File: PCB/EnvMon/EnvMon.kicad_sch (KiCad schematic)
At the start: 40 parts, among them J1 USB-C, J2 DC, J3 TEMP, J4 Shelly, M1 OLED1.5-RGB, SW1 SW_Push, SW2 SW_Push, SW3 SW_Push, U1 LMR16006XDDCR, U2 SCD41, U3 FT231XQ, U4 ESP32-PICO-MINI-02, U5 QR, U7 SHT40, U8 VEML6040

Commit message: One board
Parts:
- removed C1: 100nF, RevK:C_0603_, symbol RevK:Hidden
- removed C2: 2.2uF, RevK:C_0805_, symbol RevK:Hidden
- removed C3: 10uF, RevK:C_0805_, symbol RevK:Hidden
- removed C4: 10nF, RevK:C_0603, symbol Device:C
- removed D1: Schottky, RevK:D_1206_, symbol RevK:Hidden
- removed D3: LED_BARG, RevK:MHS190RGBCT, symbol Device:LED_BARG
- removed D4: D, RevK:D_1206, symbol Device:D
- removed J4: Shelly, RevK:Shelly, symbol RevK:Shelly
- removed L1: 6.8uH, RevK:L_4x4_, symbol RevK:Hidden
- removed R10: 4k7, RevK:R_0603, symbol Device:R
- removed R11, R12: 10k, RevK:R_0603, symbol Device:R
- removed R6: 27R, RevK:R_0603, symbol Device:R
- removed R7: 300R, RevK:R_0603, symbol Device:R
- removed R8: 1K, RevK:R_0603, symbol Device:R
- removed R9: 100R, RevK:R_0603, symbol Device:R
- removed U1: LMR16006XDDCR, RevK:SOT-23-Thin-6-Reg, symbol RevK:LMR16006XDDCR
- removed U3: FT231XQ, RevK:QFN-20-1EP_4x4mm_P0.5mm_EP2.5x2.5mm, symbol RevK:FT231XQ
- removed U4: ESP32-PICO-MINI-02, RevK:ESP32-PICO-MINI-02, symbol RevK:ESP32-PICO-MINI-02
- added C1: 100nF, RevK:C_0402, symbol Device:C
- added C2: 22uF, RevK:C_0402, symbol Device:C
- added C3: 1uF, RevK:C_0402, symbol Device:C
- added C6: 10uF 50V, RevK:C_0603_, symbol RevK:Hidden
- added C7: 10uF 6.3V, RevK:C_0603_, symbol RevK:Hidden
- added C8: 100nF, RevK:C_0603_, symbol RevK:Hidden
- added D1: RGB, RevK:LED-RGB-1.6x1.6, symbol Device:LED_RGBA
- added D3: D, RevK:D_SOD-123, symbol Device:D
- added J5: Shelly, RevK:Shelly, symbol RevK:Shelly
- added L2: 10uH, RevK:L_4x4_, symbol RevK:Hidden
- added R14: 124k, RevK:R_0402_, symbol RevK:Hidden
- added R15: 39k2, RevK:R_0402_, symbol RevK:Hidden
- added R16: 1M, RevK:R_0402_, symbol RevK:Hidden
- added R17: 220R, RevK:R_0402, symbol Device:R
- added U1: ESP32-S3-MINI-1, RevK:ESP32-S3-MINI-1, symbol RevK:ESP32-S3-MINI-1-N4R2
- added U6: MD8942, RevK:SOT-23-6-MD8942, symbol RevK:MD89420-RegBlock
- C5: footprint RevK:C_0603 -> RevK:C_0402
- D2: footprint RevK:D_1206 -> RevK:D_SOD-123; LCSC Part # C143805 -> C1884542
- R1: value 100k 1% -> 680R; footprint RevK:R_0603 -> RevK:R_0402; LCSC Part # C14675 -> (none)
- R13, R3, R4: footprint RevK:R_0603 -> RevK:R_0402
- R2: value 30k 1% -> 2K; footprint RevK:R_0603 -> RevK:R_0402; LCSC Part # C100001 -> (none)
- R5: value 27R -> 10K; footprint RevK:R_0603 -> RevK:R_0402
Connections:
- net +3.3V: now also R5.1, C1.1, C2.1, D1.4 (A), J5.3 (3V3), U1.3 (3V3), U6.8 (VOUT); no longer R1.1
- net B: now also R17.2, U1.38 (GPIO42)
- net BUTTON1: now also U1.8 (GPIO4)
- net BUTTON2: now also U1.9 (GPIO5)
- net BUTTON3: now also U1.10 (GPIO6)
- net D+: now also J1.A6 (D+), J1.B6 (D+), U1.24 (GPIO20)
- net D-: now also J1.A7 (D-), J1.B7 (D-), U1.23 (GPIO19); no longer R5.2
- net DC: now also D3.1 (K), U6.5 (VIN)
- net G: now also R2.2, U1.36 (GPIO40)
- net GND: now also C1.2, C2.2, C3.2, J5.1 (GND), U1.1 (GND), U1.2 (GND), U1.42 (GND), U1.43 (GND), U1.46 (GND), U1.47 (GND), U1.48 (GND), U1.49 (GND), U1.50 (GND), U1.51 (GND), U1.52 (GND), U1.53 (GND), U1.54 (GND), U1.55 (GND), U1.56 (GND), U1.57 (GND), U1.58 (GND), U1.59 (GND), U1.60 (GND), U1.61 (GND), U1.62 (GND), U1.63 (GND), U1.64 (GND), U1.65 (GND), U6.2 (GND), U6.7 (GND); no longer R2.1
- net OLED-CS: now also U1.13 (GPIO9)
- net OLED-DC: now also U1.14 (GPIO10)
- net OLED-MOSI: now also U1.11 (GPIO7)
- net OLED-RST: now also U1.15 (GPIO11)
- net OLED-SCK: now also U1.12 (GPIO8)
- net R: now also R1.2, U1.37 (GPIO41)
- net SCL: now also U1.34 (GPIO38)
- net SDA: now also U1.35 (GPIO39)
- net TEMP: now also U1.16 (GPIO12)
- net at J2.2 (DC): now also D2.2 (A)
- net VBUS: no longer names the net of J1.A4 (VBUS), J1.A9 (VBUS), J1.B4 (VBUS), J1.B9 (VBUS)
- net VBUS: now also D3.2 (A); no longer D2.2 (A)
- new net: J5.2 (0), U1.4 (GPIO0)
- new net: J5.4 (Rx), U1.40 (GPIO44)
- new net: J5.5 (Tx), U1.39 (GPIO43)
- new net: D1.2 (GK), R2.1
- new net: C3.1, R5.2, U1.45 (EN)
- new net: D1.1 (RK), R1.1
- new net: D1.3 (BK), R17.1
- new net RX: U1.25 (GPIO21)
- new net TX: U1.27 (GPIO47)
- no-connect marks 13 -> 15

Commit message: WS2812B LED
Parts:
- removed D1: RGB, RevK:LED-RGB-1.6x1.6, symbol Device:LED_RGBA
- removed R1: 680R, RevK:R_0402, symbol Device:R
- removed R17: 220R, RevK:R_0402, symbol Device:R
- removed R2: 2K, RevK:R_0402, symbol Device:R
- added D4: XL-1010RGBC-WS2812B, RevK:SMD1010, symbol RevK:WS2812B-1mm
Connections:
- net +3.3V: now also D4.2 (+)
- net GND: now also D4.3 (-)
- net LED: now reaches U1.41 (GPIO45)
- net LED: now also D4.4 (I)
- net B: no longer names the net of U1.38 (GPIO42)
- net G: no longer names the net of U1.36 (GPIO40)
- net R: no longer names the net of U1.37 (GPIO41)
- no-connect marks 15 -> 19
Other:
- moved on the sheet: C3, R5

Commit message: New
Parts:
- removed D2: D, RevK:D_SOD-123, symbol Device:D
- added D2: Schottky, RevK:D_1206, symbol Diode:1N5819
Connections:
- net DC: now also D2.1 (K)
- net at J2.2 (DC): now also D2.2 (A)
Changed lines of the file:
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@@
-    )
-  )
-  (symbol (lib_id "Device:D") (at 44.45 123.825 0) (unit 1)
-    (in_bom yes) (on_board yes) (dnp no)
-    (property "Reference" "D2" (at 44.45 129.3368 0)
-      (effects (font (size 1.27 1.27)))
-    )
-    (property "Value" "D" (at 44.45 127.0254 0)
-      (effects (font (size 1.27 1.27)))
-    )
-    (property "Footprint" "RevK:D_SOD-123" (at 44.45 123.825 0)
-      (effects (font (size 1.27 1.27)) hide)
-    )
-    (property "Datasheet" "~" (at 44.45 123.825 0)
-      (effects (font (size 1.27 1.27)) hide)
-    )
-    (property "LCSC Part #" "C1884542" (at 44.45 123.825 0)
-      (effects (font (size 1.27 1.27)) hide)
-    )
-    (pin "1")
-    (pin "2")
-    (instances
-      (project "EnvMon"
-        (path "/12422a89-3d0c-485c-9386-f77121fd68fd"
-          (reference "D2") (unit 1)
-        )
-      )
-      (project "Access"
-        (path "/2a267270-6585-45e3-a633-b53049f10066"
-          (reference "D8") (unit 1)
-        )
-      )
-      (project "GenericS3"
-        (path "/2d210a96-f81f-42a9-8bf4-1b43c11086f3"
-          (reference "D1") (unit 1)
-        )
-      )
     )
   )
@@
         )
       )
+    )
+  )
+  (symbol (lib_id "Diode:1N5819") (at 44.45 123.825 0) (unit 1)
+    (in_bom yes) (on_board yes) (dnp no)
+    (property "Reference" "D2" (at 45.72 128.905 0)
+      (effects (font (size 1.27 1.27)))
+    )
+    (property "Value" "Schottky" (at 42.545 127 0)
+      (effects (font (size 1.27 1.27)))
+    )
+    (property "Footprint" "RevK:D_1206" (at 44.45 128.27 0)
+      (effects (font (size 1.27 1.27)) hide)
+    )
+    (property "Datasheet" "" (at 44.45 123.825 0)
+      (effects (font (size 1.27 1.27)) hide)
+    )
+    (property "LCSC Part #" "C143805" (at 44.45 123.825 0)
+      (effects (font (size 1.27 1.27)) hide)
+    )
+    (pin "1")
+    (pin "2")
+    (instances
+      (project "EnvMon"
+        (path "/12422a89-3d0c-485c-9386-f77121fd68fd"
+          (reference "D2") (unit 1)
+        )
+      )
+      (project "EPD75"
+        (path "/46c350bb-7de4-4e81-aafd-4af55e37aab0"
+          (reference "D6") (unit 1)
+        )
+      )

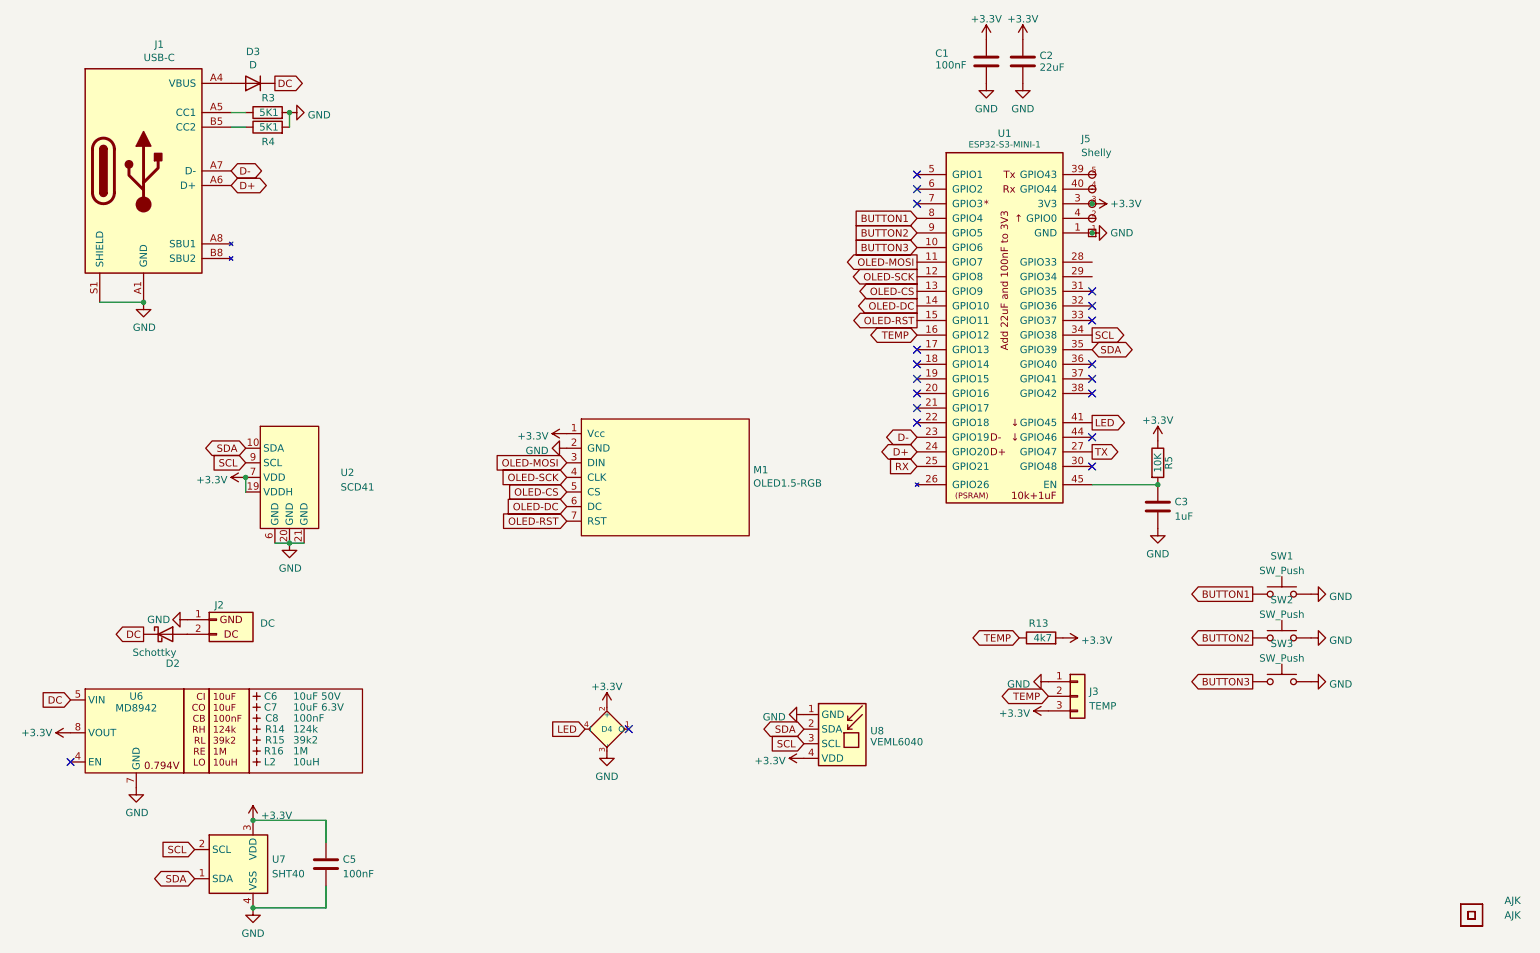
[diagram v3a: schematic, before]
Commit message: New plugs
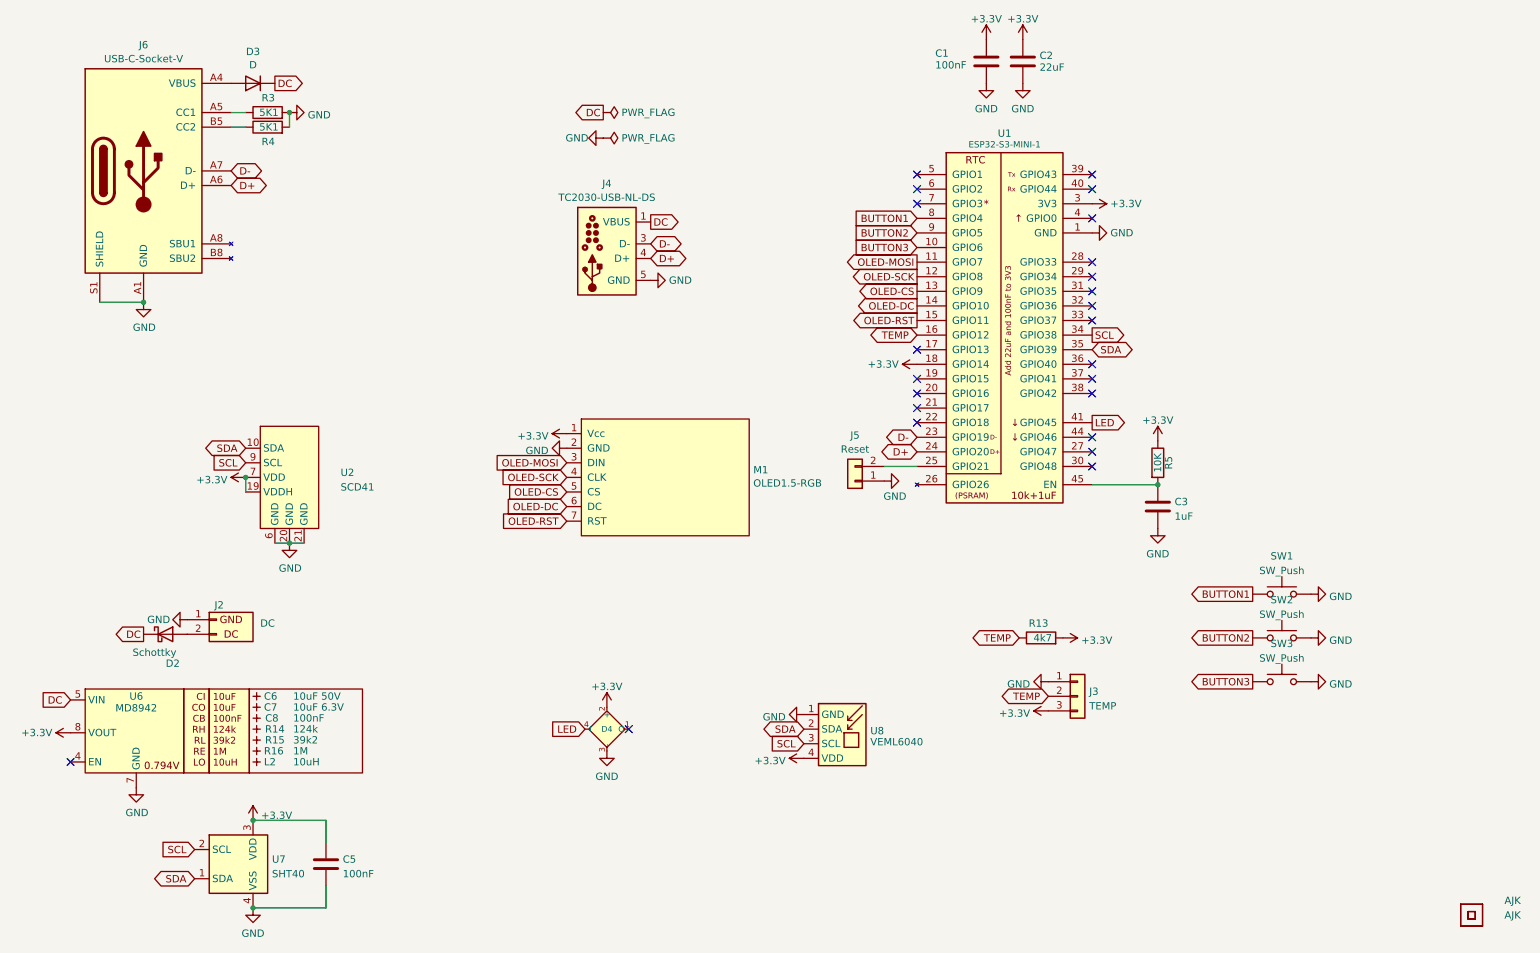
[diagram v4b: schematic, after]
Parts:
- removed J1: USB-C, RevK:USC16-TR, symbol RevK:USB-C
- removed J5: Shelly, RevK:Shelly, symbol RevK:Shelly
- added J4: TC2030-USB-NL-DS, RevK:Tag-Connect_TC2030-IDC-NL_2x03_P1.27mm_Vertical, symbol RevK:TC2030-USB-NL
- added J5: Reset, RevK:AA-Pad, symbol Connector_Generic:Conn_01x02
- added J6: USB-C-Socket-V, RevK:USB-C-Socket-H, symbol RevK:USB-C-Socket-H
- J2: footprint RevK:PTSM-HH-2-RA-W -> RevK:WAGO-2060-452-998-404
- J3: footprint RevK:PTSM-HH-3-RA -> RevK:WAGO-2060-453-998-404
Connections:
- net +3.3V: now also U1.18 (GPIO14)
- net D+: now also J4.4 (D+), J6.A6 (D+), J6.B6 (D+)
- net D-: now also J4.3 (D-), J6.A7 (D-), J6.B7 (D-)
- net DC: now also J4.1 (VBUS), J4.2 (VBUS)
- net GND: now also J4.5 (GND), J4.6 (GND), J5.1 (Pin_1), J6.A1 (GND), J6.A12 (GND), J6.B1 (GND), J6.B12 (GND), J6.S1 (SHIELD)
- net at D3.2 (A): now also J6.A4 (VBUS), J6.A9 (VBUS), J6.B4 (VBUS), J6.B9 (VBUS)
- net at R3.1: now also J6.A5 (CC1)
- net at R4.1: now also J6.B5 (CC2)
- net RX: no longer names the net of U1.25 (GPIO21)
- net RX: now also J5.2 (Pin_2)
- net TX: no longer names the net of U1.27 (GPIO47)
- no-connect marks 19 -> 24

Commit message: PCB Update
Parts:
- C6: LCSC Part # C1591 -> (none); MPN (none) -> C1591
- C7: LCSC Part # C1691 -> (none); MPN (none) -> C1691
- D2: LCSC Part # C143805 -> (none); MPN (none) -> C143805
- D3: LCSC Part # C1884542 -> (none); MPN (none) -> C1884542
- D4: LCSC Part # C5349953 -> (none); MPN (none) -> C5349953
- J6: value USB-C-Socket-V -> USB-C-Socket-H; LCSC Part # C709357 -> (none); MPN (none) -> C709357
- U1: LCSC Part # C3013941 -> (none); MPN (none) -> C3013941
- U6: LCSC Part # C2684786 -> (none); MPN (none) -> C2684786
- U7: LCSC Part # C2909890 -> (none); MPN (none) -> C2909890
- U8: JLCPCB Rotation Offset 90 -> (none); LCSC Part # C78465 -> (none); MPN (none) -> C78465
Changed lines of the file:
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@@
 (kicad_sch
-	(version 20231120)
+	(version 20241209)
 	(generator "eeschema")
-	(generator_version "8.0")
+	(generator_version "9.0")
 	(paper "A4")
 	(title_block
@@
 			)
 		)
-		(property "LCSC Part #" "C2684786"
+		(property "MPN" "C2684786"
 			(at 39.37 167.64 0)
 			(effects
@@
 			)
 		)
-		(property "LCSC Part #" "C1591"
+		(property "MPN" "C1591"
 			(at 60.325 134.62 0)
 			(effects
@@
 			)
 		)
-		(property "LCSC Part #" "C5349953"
+		(property "MPN" "C5349953"
 			(at 122.555 128.905 0)
 			(effects
@@
 			)
 		)
-		(property "LCSC Part #" "C143805"
+		(property "MPN" "C143805"
 			(at 44.45 123.825 0)
 			(effects
@@
 			)
 		)
-		(property "LCSC Part #" "C1884542"
+		(property "MPN" "C1884542"
 			(at 59.69 27.94 0)
 			(effects
@@
 			)
 		)
-		(property "Value" "USB-C-Socket-V"
+		(property "Value" "USB-C-Socket-H"
 			(at 40.64 23.6798 0)
 			(effects
@@
 			)
 		)
-		(property "LCSC Part #" "C709357"
+		(property "MPN" "C709357"
 			(at 40.64 43.18 0)
 			(effects
@@
 			)
 		)
-		(property "LCSC Part #" "C78465"
+		(property "MPN" "C78465"
 			(at 162.56 150.495 0)
 			(effects
@@
 			)
 		)
-		(property "JLCPCB Rotation Offset" "90"
-			(at 162.56 152.4 0)
-			(effects
-				(font
-					(size 1.27 1.27)
-				)
-				(hide yes)
-			)
-		)
 		(pin "1"
 		)
@@
 			)
 		)
-		(property "LCSC Part #" "C3013941"
+		(property "MPN" "C3013941"
 			(at 190.5 102.87 0)
 			(effects
@@
 			)
 		)
-		(property "LCSC Part #" "C1691"
+		(property "MPN" "C1691"
 			(at 60.325 136.525 0)
 			(effects
@@
 			)
 		)
-		(property "LCSC Part #" "C2909890"
+		(property "MPN" "C2909890"
 			(at 62.992 166.8007 0)
 			(effects
@@
 		)
 	)
+	(embedded_fonts no)
 )
